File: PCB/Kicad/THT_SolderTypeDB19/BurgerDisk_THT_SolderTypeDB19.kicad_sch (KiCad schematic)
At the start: 15 parts, among them J1 Daisy port in, J2 MicroSD module, J3 UART, J4 Daisy port out, U1 PC817

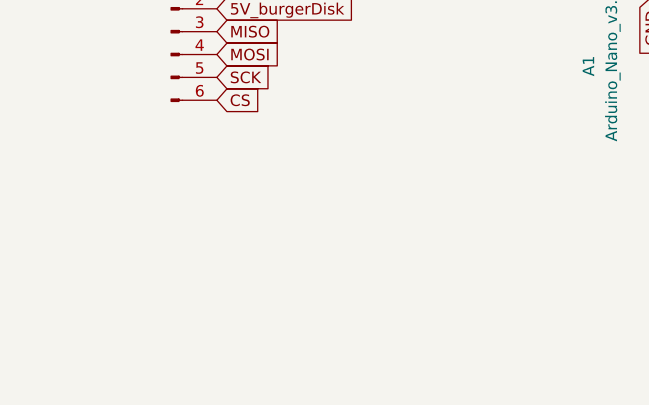
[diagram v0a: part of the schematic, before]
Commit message: Add 8-pin header for full size SD module
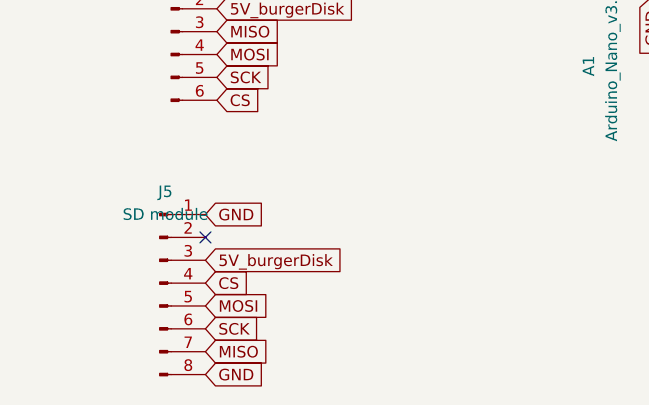
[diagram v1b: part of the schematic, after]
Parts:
- added J5: SD module, Connector_PinHeader_2.54mm:PinHeader_1x08_P2.54mm_Vertical, symbol Connector:Conn_01x08_Pin
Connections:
- net 5V_burgerDisk: now also J5.3 (Pin_3)
- net CS: now also J5.4 (Pin_4)
- net GND: now also J5.1 (Pin_1), J5.8 (Pin_8)
- net MISO: now also J5.7 (Pin_7)
- net MOSI: now also J5.5 (Pin_5)
- net SCK: now also J5.6 (Pin_6)
- no-connect marks 9 -> 10
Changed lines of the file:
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@@
   (no_connect (at 165.1 120.65))
   (no_connect (at 165.1 87.63))
+  (no_connect (at 102.87 154.94))
   (no_connect (at 165.1 97.79))
   (no_connect (at 139.7 87.63))
@@
     )
   )
+  (global_label "MISO" (shape input) (at 102.87 167.64 0) (fields_autoplaced)
+    (effects (font (size 1.27 1.27)) (justify left))
+    (property "Intersheetrefs" "${INTERSHEET_REFS}" (at 110.4514 167.64 0)
+      (effects (font (size 1.27 1.27)) (justify left) hide)
+    )
+  )
   (global_label "5V_burgerDisk" (shape input) (at 157.48 74.93 0) (fields_autoplaced)
     (effects (font (size 1.27 1.27)) (justify left))
@@
     )
   )
+  (global_label "MOSI" (shape input) (at 102.87 162.56 0) (fields_autoplaced)
+    (effects (font (size 1.27 1.27)) (justify left))
+    (property "Intersheetrefs" "${INTERSHEET_REFS}" (at 110.4514 162.56 0)
+      (effects (font (size 1.27 1.27)) (justify left) hide)
+    )
+  )
   (global_label "PH0" (shape input) (at 228.6 88.9 180) (fields_autoplaced)
     (effects (font (size 1.27 1.27)) (justify right))
@@
     )
   )
+  (global_label "GND" (shape input) (at 102.87 170.18 0) (fields_autoplaced)
+    (effects (font (size 1.27 1.27)) (justify left))
+    (property "Intersheetrefs" "${INTERSHEET_REFS}" (at 109.7257 170.18 0)
+      (effects (font (size 1.27 1.27)) (justify left) hide)
+    )
+  )
   (global_label "DRV1_in" (shape input) (at 137.16 41.91 0) (fields_autoplaced)
     (effects (font (size 1.27 1.27)) (justify left))
@@
     )
   )
+  (global_label "5V_burgerDisk" (shape input) (at 102.87 157.48 0) (fields_autoplaced)
+    (effects (font (size 1.27 1.27)) (justify left))
+    (property "Intersheetrefs" "${INTERSHEET_REFS}" (at 119.1599 157.48 0)
+      (effects (font (size 1.27 1.27)) (justify left) hide)
+    )
+  )
   (global_label "-12V" (shape input) (at 124.46 36.83 180) (fields_autoplaced)
     (effects (font (size 1.27 1.27)) (justify right))
@@
     )
   )
+  (global_label "CS" (shape input) (at 102.87 160.02 0) (fields_autoplaced)
+    (effects (font (size 1.27 1.27)) (justify left))
+    (property "Intersheetrefs" "${INTERSHEET_REFS}" (at 108.3347 160.02 0)
+      (effects (font (size 1.27 1.27)) (justify left) hide)
+    )
+  )
   (global_label "WREQ" (shape input) (at 228.6 109.22 180) (fields_autoplaced)
     (effects (font (size 1.27 1.27)) (justify right))
@@
     (property "Intersheetrefs" "${INTERSHEET_REFS}" (at 115.9715 34.29 0)
       (effects (font (size 1.27 1.27)) (justify right) hide)
+    )
+  )
+  (global_label "GND" (shape input) (at 102.87 152.4 0) (fields_autoplaced)
+    (effects (font (size 1.27 1.27)) (justify left))
+    (property "Intersheetrefs" "${INTERSHEET_REFS}" (at 109.7257 152.4 0)
+      (effects (font (size 1.27 1.27)) (justify left) hide)
+    )
+  )
+  (global_label "SCK" (shape input) (at 102.87 165.1 0) (fields_autoplaced)
+    (effects (font (size 1.27 1.27)) (justify left))
+    (property "Intersheetrefs" "${INTERSHEET_REFS}" (at 109.6047 165.1 0)
+      (effects (font (size 1.27 1.27)) (justify left) hide)
     )
   )
@@
         )
       )
+    )
+  )
+  (symbol (lib_id "Connector:Conn_01x08_Pin") (at 97.79 160.02 0) (unit 1)
+    (in_bom yes) (on_board yes) (dnp no)
+    (property "Reference" "J5" (at 98.425 149.86 0)
+      (effects (font (size 1.27 1.27)))
+    )
+    (property "Value" "SD module" (at 98.425 152.4 0)
+      (effects (font (size 1.27 1.27)))
+    )
+    (property "Footprint" "Connector_PinHeader_2.54mm:PinHeader_1x08_P2.54mm_Vertical" (at 97.79 160.02 0)
+      (effects (font (size 1.27 1.27)) hide)
+    )
+    (property "Datasheet" "~" (at 97.79 160.02 0)
+      (effects (font (size 1.27 1.27)) hide)
+    )
+    (property "LCSC" "C6209271" (at 97.79 160.02 0)
+      (effects (font (size 1.27 1.27)) hide)
+    )
+    (pin "4")
+    (pin "5")
+    (pin "3")
+    (pin "6")
+    (pin "1")
+    (pin "2")
+    (pin "7")
+    (pin "8")
+    (instances
+      (project "BurgerDisk_THT_SolderTypeDB19"
+        (path "/596d0583-1d97-453e-b84c-75eed809afa2"
+          (reference "J5") (unit 1)
+        )
+      )

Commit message: Vertical footprints
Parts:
- J2: footprint Connector_PinHeader_2.54mm:PinHeader_1x06_P2.54mm_Horizontal -> Connector_PinHeader_2.54mm:PinHeader_1x06_P2.54mm_Vertical
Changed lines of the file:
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@@
       (effects (font (size 1.27 1.27)))
     )
-    (property "Footprint" "Connector_PinHeader_2.54mm:PinHeader_1x06_P2.54mm_Horizontal" (at 99.06 132.08 0)
+    (property "Footprint" "Connector_PinHeader_2.54mm:PinHeader_1x06_P2.54mm_Vertical" (at 99.06 132.08 0)
       (effects (font (size 1.27 1.27)) hide)
     )

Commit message: Add a very hacky way to add Nano headers
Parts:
- J5: LCSC C6209271 -> C124381
- R3: LCSC C61239 -> C129899
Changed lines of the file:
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@@
       (effects (font (size 1.27 1.27)) hide)
     )
-    (property "LCSC" "C61239" (at 99.06 68.58 0)
+    (property "LCSC" "C129899" (at 99.06 68.58 0)
       (effects (font (size 1.27 1.27)) hide)
     )
@@
       (effects (font (size 1.27 1.27)) hide)
     )
-    (property "LCSC" "C6209271" (at 97.79 160.02 0)
-      (effects (font (size 1.27 1.27)) hide)
-    )
+    (property "LCSC" "C124381" (at 97.79 160.02 0)
+      (effects (font (size 1.27 1.27)) hide)
+    )

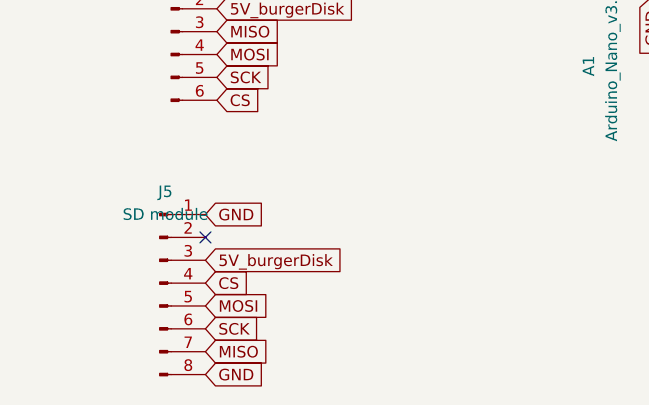
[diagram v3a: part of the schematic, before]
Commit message: Revert full-size SD connector and module.
They don't have level shifter.
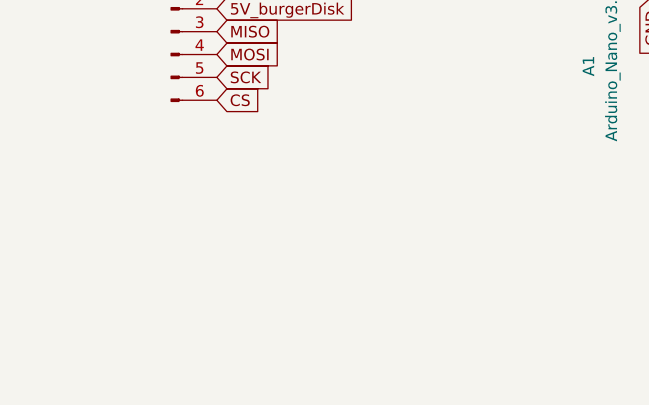
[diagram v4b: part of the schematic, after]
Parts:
- removed J5: SD module, Connector_PinHeader_2.54mm:PinHeader_1x08_P2.54mm_Vertical, symbol Connector:Conn_01x08_Pin
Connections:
- no-connect marks 10 -> 9
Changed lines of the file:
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@@
   (no_connect (at 165.1 120.65))
   (no_connect (at 165.1 87.63))
-  (no_connect (at 102.87 154.94))
   (no_connect (at 165.1 97.79))
   (no_connect (at 139.7 87.63))
@@
     )
   )
-  (global_label "MISO" (shape input) (at 102.87 167.64 0) (fields_autoplaced)
-    (effects (font (size 1.27 1.27)) (justify left))
-    (property "Intersheetrefs" "${INTERSHEET_REFS}" (at 110.4514 167.64 0)
-      (effects (font (size 1.27 1.27)) (justify left) hide)
-    )
-  )
   (global_label "5V_burgerDisk" (shape input) (at 157.48 74.93 0) (fields_autoplaced)
     (effects (font (size 1.27 1.27)) (justify left))
@@
     )
   )
-  (global_label "MOSI" (shape input) (at 102.87 162.56 0) (fields_autoplaced)
-    (effects (font (size 1.27 1.27)) (justify left))
-    (property "Intersheetrefs" "${INTERSHEET_REFS}" (at 110.4514 162.56 0)
-      (effects (font (size 1.27 1.27)) (justify left) hide)
-    )
-  )
   (global_label "PH0" (shape input) (at 228.6 88.9 180) (fields_autoplaced)
     (effects (font (size 1.27 1.27)) (justify right))
@@
     )
   )
-  (global_label "GND" (shape input) (at 102.87 170.18 0) (fields_autoplaced)
-    (effects (font (size 1.27 1.27)) (justify left))
-    (property "Intersheetrefs" "${INTERSHEET_REFS}" (at 109.7257 170.18 0)
-      (effects (font (size 1.27 1.27)) (justify left) hide)
-    )
-  )
   (global_label "DRV1_in" (shape input) (at 137.16 41.91 0) (fields_autoplaced)
     (effects (font (size 1.27 1.27)) (justify left))
@@
     )
   )
-  (global_label "5V_burgerDisk" (shape input) (at 102.87 157.48 0) (fields_autoplaced)
-    (effects (font (size 1.27 1.27)) (justify left))
-    (property "Intersheetrefs" "${INTERSHEET_REFS}" (at 119.1599 157.48 0)
-      (effects (font (size 1.27 1.27)) (justify left) hide)
-    )
-  )
   (global_label "-12V" (shape input) (at 124.46 36.83 180) (fields_autoplaced)
     (effects (font (size 1.27 1.27)) (justify right))
@@
     )
   )
-  (global_label "CS" (shape input) (at 102.87 160.02 0) (fields_autoplaced)
-    (effects (font (size 1.27 1.27)) (justify left))
-    (property "Intersheetrefs" "${INTERSHEET_REFS}" (at 108.3347 160.02 0)
-      (effects (font (size 1.27 1.27)) (justify left) hide)
-    )
-  )
   (global_label "WREQ" (shape input) (at 228.6 109.22 180) (fields_autoplaced)
     (effects (font (size 1.27 1.27)) (justify right))
@@
     (property "Intersheetrefs" "${INTERSHEET_REFS}" (at 115.9715 34.29 0)
       (effects (font (size 1.27 1.27)) (justify right) hide)
-    )
-  )
-  (global_label "GND" (shape input) (at 102.87 152.4 0) (fields_autoplaced)
-    (effects (font (size 1.27 1.27)) (justify left))
-    (property "Intersheetrefs" "${INTERSHEET_REFS}" (at 109.7257 152.4 0)
-      (effects (font (size 1.27 1.27)) (justify left) hide)
-    )
-  )
-  (global_label "SCK" (shape input) (at 102.87 165.1 0) (fields_autoplaced)
-    (effects (font (size 1.27 1.27)) (justify left))
-    (property "Intersheetrefs" "${INTERSHEET_REFS}" (at 109.6047 165.1 0)
-      (effects (font (size 1.27 1.27)) (justify left) hide)
     )
   )
@@
         )
       )
-    )
-  )
-  (symbol (lib_id "Connector:Conn_01x08_Pin") (at 97.79 160.02 0) (unit 1)
-    (in_bom yes) (on_board yes) (dnp no)
-    (property "Reference" "J5" (at 98.425 149.86 0)
-      (effects (font (size 1.27 1.27)))
-    )
-    (property "Value" "SD module" (at 98.425 152.4 0)
-      (effects (font (size 1.27 1.27)))
-    )
-    (property "Footprint" "Connector_PinHeader_2.54mm:PinHeader_1x08_P2.54mm_Vertical" (at 97.79 160.02 0)
-      (effects (font (size 1.27 1.27)) hide)
-    )
-    (property "Datasheet" "~" (at 97.79 160.02 0)
-      (effects (font (size 1.27 1.27)) hide)
-    )
-    (property "LCSC" "C124381" (at 97.79 160.02 0)
-      (effects (font (size 1.27 1.27)) hide)
-    )
-    (pin "4")
-    (pin "5")
-    (pin "3")
-    (pin "6")
-    (pin "1")
-    (pin "2")
-    (pin "7")
-    (pin "8")
-    (instances
-      (project "BurgerDisk_THT_SolderTypeDB19"
-        (path "/596d0583-1d97-453e-b84c-75eed809afa2"
-          (reference "J5") (unit 1)
-        )
-      )
